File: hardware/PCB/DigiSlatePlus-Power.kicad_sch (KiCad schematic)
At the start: 38 parts, among them J3 +8-24 Volt, J4 Battery, J5 Mains, Q3 FS8205A, U21 LM2596S-ADJ, U22 DW01A, U23 TP4056, U24 KA78M05_TO252, U25 LD1117S33TR_SOT223

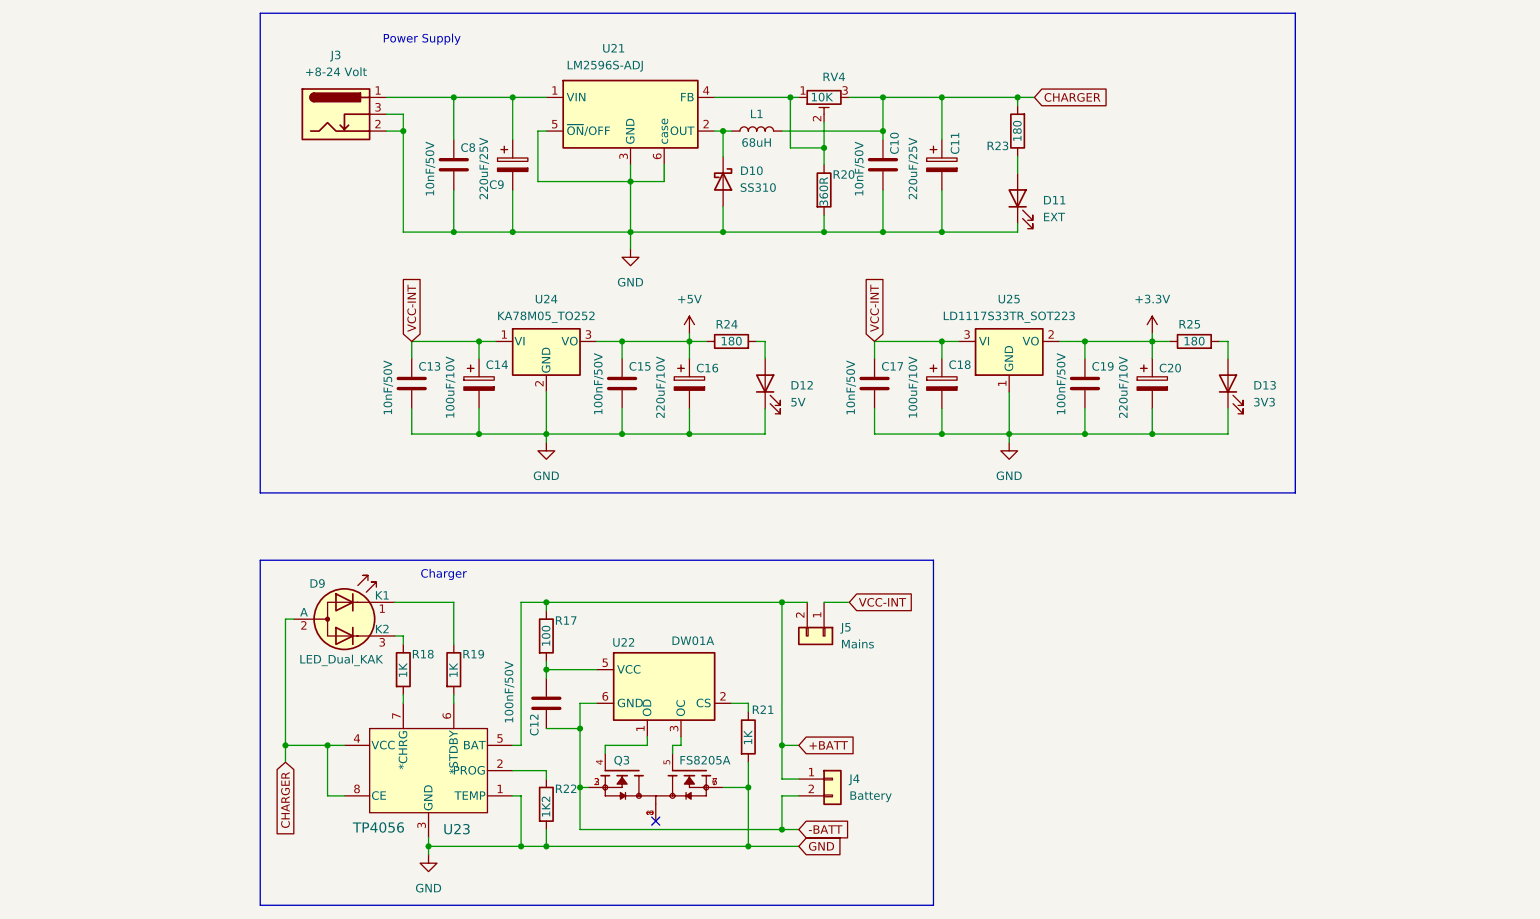
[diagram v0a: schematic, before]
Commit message: first finished schematic version
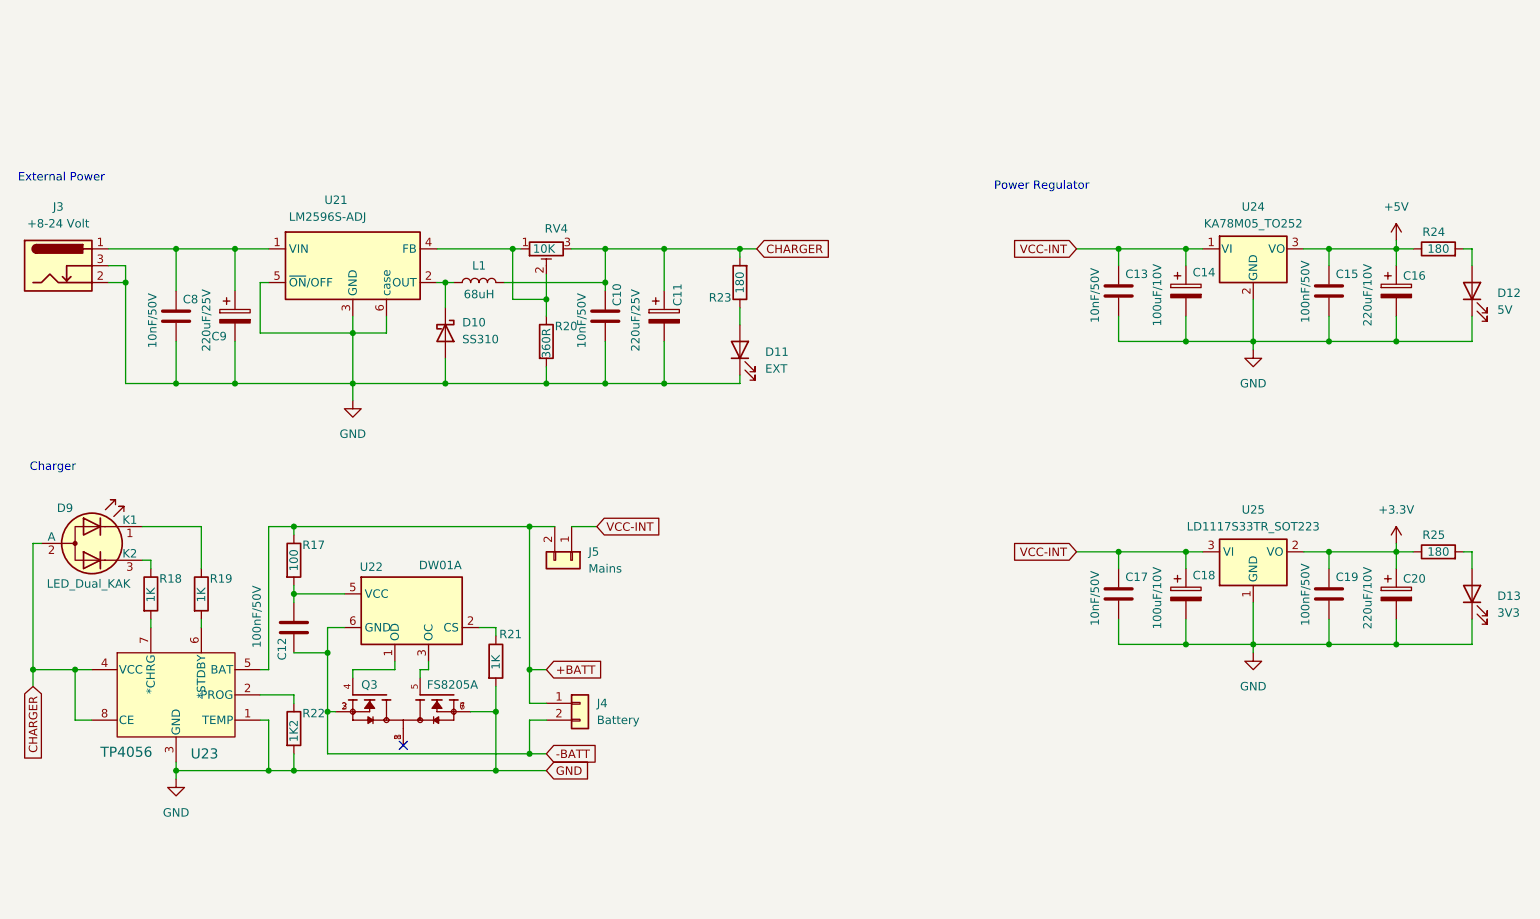
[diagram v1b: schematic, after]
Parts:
- D11: footprint LED_SMD:LED_0201_0603Metric_Pad0.64x0.40mm_HandSolder -> LED_THT:LED_D3.0mm
- D12, D13: footprint LED_SMD:LED_0201_0603Metric_Pad0.64x0.40mm_HandSolder -> LED_SMD:LED_0603_1608Metric
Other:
- note added: "External Power"
- note added: "Power Regulator"
- note removed: "Power Supply"
- moved on the sheet: C10, C11, C12, C13, C14, C15, C16, C17, C18, C19, C20, C8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

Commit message: final 1.0 board version
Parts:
- removed J5: Mains, Connector_JST:JST_XH_B2B-XH-AM_1x02_P2.50mm_Vertical, symbol Connector_Generic:Conn_01x02
- added SW7: SW_DPDT_x2, Button_Switch_THT:SW_Slide_SPDT_Angled_CK_OS102011MA1Q, symbol Switch:SW_DPDT_x2
- U21: footprint Package_TO_SOT_SMD:TO-263-5_TabPin6 -> Package_TO_SOT_SMD:TO-263-5_TabPin3
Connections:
- net +BATT: now also SW7.2 (B)
- net GND: no longer U21.6 (case)
- net VCC-INT: now also SW7.3 (C)
- no-connect marks 1 -> 2
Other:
- title: (none) -> DigiSlate+
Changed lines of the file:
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@@
 	(generator_version "8.0")
 	(paper "A4")
+	(title_block
+		(title "DigiSlate+")
+		(date "2024-09-05")
+		(rev "1.0")
+	)
 	(junction
 		(at 228.6 69.85)
@@
 	)
 	(no_connect
+		(at 121.92 109.22)
+	)
+	(no_connect
 		(at 88.9 144.78)
 	)
@@
 	(wire
 		(pts
-			(xy 118.11 111.76) (xy 114.3 111.76)
+			(xy 125.73 114.3) (xy 121.92 114.3)
 		)
 		(stroke
@@
 	(global_label "VCC-INT"
 		(shape input)
-		(at 118.11 111.76 0)
+		(at 125.73 114.3 0)
 		(fields_autoplaced yes)
 		(effects
@@
 		)
 		(property "Intersheetrefs" "${INTERSHEET_REFS}"
-			(at 129.1991 111.76 0)
+			(at 136.8191 114.3 0)
 			(effects
 				(font
@@
 			)
 		)
-		(property "Footprint" "Package_TO_SOT_SMD:TO-263-5_TabPin6"
+		(property "Footprint" "Package_TO_SOT_SMD:TO-263-5_TabPin3"
 			(at 82.55 78.74 0)
 			(effects
@@
 		(pin "2"
 		)
-		(pin "6"
-		)
 		(instances
 			(project "DigiSlatePlus"
@@
 	)
 	(symbol
+		(lib_id "Switch:SW_DPDT_x2")
+		(at 116.84 111.76 0)
+		(unit 1)
+		(exclude_from_sim no)
+		(in_bom yes)
+		(on_board yes)
+		(dnp no)
+		(fields_autoplaced yes)
+		(property "Reference" "SW7"
+			(at 116.84 102.87 0)
+			(effects
+				(font
+					(size 1.27 1.27)
+				)
+			)
+		)
+		(property "Value" "SW_DPDT_x2"
+			(at 116.84 105.41 0)
+			(effects
+				(font
+					(size 1.27 1.27)
+				)
+			)
+		)
+		(property "Footprint" "Button_Switch_THT:SW_Slide_SPDT_Angled_CK_OS102011MA1Q"
+			(at 116.84 111.76 0)
+			(effects
+				(font
+					(size 1.27 1.27)
+				)
+				(hide yes)
+			)
+		)
+		(property "Datasheet" "~"
+			(at 116.84 111.76 0)
+			(effects
+				(font
+					(size 1.27 1.27)
+				)
+				(hide yes)
+			)
+		)
+		(property "Description" "Switch, dual pole double throw, separate symbols"
+			(at 116.84 111.76 0)
+			(effects
+				(font
+					(size 1.27 1.27)
+				)
+				(hide yes)
+			)
+		)
+		(pin "3"
+		)
+		(pin "4"
+		)
+		(pin "5"
+		)
+		(pin "6"
+		)
+		(pin "1"
+		)
+		(pin "2"
+		)
+		(instances
+			(project ""
+				(path "/dcb9cf24-5afa-4bbe-8afa-a00529143e4d/8d8c6cc3-ae5a-4a9a-87ce-71fd40365acc"
+					(reference "SW7")
+					(unit 1)
+				)
+			)
+		)
+	)
+	(symbol
 		(lib_id "Device:C")
 		(at 228.6 121.92 0)
@@
 					(unit 1)
 				)
-			)
-		)
-	)
-	(symbol
-		(lib_id "Connector_Generic:Conn_01x02")
-		(at 114.3 116.84 270)
-		(unit 1)
-		(exclude_from_sim no)
-		(in_bom yes)
-		(on_board yes)
-		(dnp no)
-		(fields_autoplaced yes)
-		(property "Reference" "J5"
-			(at 116.84 115.5699 90)
-			(effects
-				(font
-					(size 1.27 1.27)
-				)
-				(justify left)
-			)
-		)
-		(property "Value" "Mains"
-			(at 116.84 118.1099 90)
-			(effects
-				(font
-					(size 1.27 1.27)
-				)
-				(justify left)
-			)
-		)
-		(property "Footprint" "Connector_JST:JST_XH_B2B-XH-AM_1x02_P2.50mm_Vertical"
-			(at 114.3 116.84 0)
-			(effects
-				(font
-					(size 1.27 1.27)
-				)
-				(hide yes)
-			)
-		)
-		(property "Datasheet" "~"
-			(at 114.3 116.84 0)
-			(effects
-				(font
-					(size 1.27 1.27)
-				)
-				(hide yes)
-			)
-		)
-		(property "Description" "Generic connector, single row, 01x02, script generated (kicad-library-utils/schlib/autogen/connector/)"
-			(at 114.3 116.84 0)
-			(effects
-				(font
-					(size 1.27 1.27)
-				)
-				(hide yes)
-			)
-		)
-		(pin "2"
-		)
-		(pin "1"
-		)
-		(instances
-			(project "DigiSlatePlus"
-				(path "/dcb9cf24-5afa-4bbe-8afa-a00529143e4d/8d8c6cc3-ae5a-4a9a-87ce-71fd40365acc"
-					(reference "J5")
-					(unit 1)
-				)
